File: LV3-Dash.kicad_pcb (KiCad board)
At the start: 2 copper layers, 90 x 50 mm, 93 parts, among them J1 USB_C_Receptacle_USB2.0_16P, J2 FTSH-105-01-L-DV-K-A, J3 Conn_01x04_MountingPin, J4 Conn_01x05_Pin, J5 Conn_01x05_MountingPin, J6 MSD-11-A, J7 62684-401100AHLF, U1 STM32H743VITx, U2 TJA1051T-3, U4 LMR51625YDDCR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

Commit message: more preliminary routing, critical ground
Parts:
- moved D7 0.70 mm to (133.1, 78.4)
- moved F2 0.70 mm to (129.6, 81.6)
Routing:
- net GND: track 0.00 -> 163.3 mm
- net USB-: track 6.85 -> 104.8 mm, vias 1 -> 3
- net USB+: track 5.72 -> 101.4 mm, vias 1 -> 3
- net +3.3V: track 58.1 -> 67.1 mm
- net +5V_BUS: track 32.4 -> 37.2 mm
- net +5V_BUCK: track 13.8 -> 16.0 mm
- net +5V_USB: track 89.0 -> 89.8 mm

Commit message: finalized schematic, some routing
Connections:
- U1 pad 40: unconnected-(U1-PE10-Pad40) -> LCD_EN
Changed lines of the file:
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@@
 	(net 102 "unconnected-(U1-PB5-Pad91)")
 	(net 103 "unconnected-(U1-PE5-Pad4)")
-	(net 104 "unconnected-(U1-PE10-Pad40)")
-	(net 105 "unconnected-(U1-PE7-Pad37)")
-	(net 106 "unconnected-(U1-PB2-Pad36)")
-	(net 107 "unconnected-(U1-PE8-Pad38)")
-	(net 108 "unconnected-(U1-PC14-Pad8)")
-	(net 109 "unconnected-(U1-PA9-Pad68)")
-	(net 110 "unconnected-(U1-PE1-Pad98)")
-	(net 111 "FDCAN2_RX")
-	(net 112 "FDCAN2_TX")
-	(net 113 "unconnected-(U5-NC-Pad4)")
+	(net 104 "unconnected-(U1-PE7-Pad37)")
+	(net 105 "unconnected-(U1-PB2-Pad36)")
+	(net 106 "unconnected-(U1-PE8-Pad38)")
+	(net 107 "unconnected-(U1-PC14-Pad8)")
+	(net 108 "unconnected-(U1-PA9-Pad68)")
+	(net 109 "unconnected-(U1-PE1-Pad98)")
+	(net 110 "FDCAN2_RX")
+	(net 111 "FDCAN2_TX")
+	(net 112 "unconnected-(U5-NC-Pad4)")
 	(footprint "Connector_USB:USB_C_Receptacle_HRO_TYPE-C-31-M-12"
 		(layer "F.Cu")
@@
 			(layers "B.Cu" "B.Mask" "B.Paste")
 			(roundrect_rratio 0.25)
-			(net 108 "unconnected-(U1-PC14-Pad8)")
+			(net 107 "unconnected-(U1-PC14-Pad8)")
 			(pinfunction "PC14")
 			(pintype "bidirectional+no_connect")
@@
 			(layers "B.Cu" "B.Mask" "B.Paste")
 			(roundrect_rratio 0.25)
-			(net 106 "unconnected-(U1-PB2-Pad36)")
+			(net 105 "unconnected-(U1-PB2-Pad36)")
 			(pinfunction "PB2")
 			(pintype "bidirectional+no_connect")
@@
 			(layers "B.Cu" "B.Mask" "B.Paste")
 			(roundrect_rratio 0.25)
-			(net 105 "unconnected-(U1-PE7-Pad37)")
+			(net 104 "unconnected-(U1-PE7-Pad37)")
 			(pinfunction "PE7")
 			(pintype "bidirectional+no_connect")
@@
 			(layers "B.Cu" "B.Mask" "B.Paste")
 			(roundrect_rratio 0.25)
-			(net 107 "unconnected-(U1-PE8-Pad38)")
+			(net 106 "unconnected-(U1-PE8-Pad38)")
 			(pinfunction "PE8")
 			(pintype "bidirectional+no_connect")
@@
 			(layers "B.Cu" "B.Mask" "B.Paste")
 			(roundrect_rratio 0.25)
-			(net 104 "unconnected-(U1-PE10-Pad40)")
+			(net 76 "LCD_EN")
 			(pinfunction "PE10")
-			(pintype "bidirectional+no_connect")
+			(pintype "bidirectional")
 		)
 		(pad "41" smd roundrect
@@
 			(layers "B.Cu" "B.Mask" "B.Paste")
 			(roundrect_rratio 0.25)
-			(net 111 "FDCAN2_RX")
+			(net 110 "FDCAN2_RX")
 			(pinfunction "PB12")
 			(pintype "bidirectional")
@@
 			(layers "B.Cu" "B.Mask" "B.Paste")
 			(roundrect_rratio 0.25)
-			(net 109 "unconnected-(U1-PA9-Pad68)")
+			(net 108 "unconnected-(U1-PA9-Pad68)")
 			(pinfunction "PA9")
 			(pintype "bidirectional+no_connect")
@@
 			(layers "B.Cu" "B.Mask" "B.Paste")
 			(roundrect_rratio 0.25)
-			(net 112 "FDCAN2_TX")
+			(net 111 "FDCAN2_TX")
 			(pinfunction "PB6")
 			(pintype "bidirectional")
@@
 			(layers "B.Cu" "B.Mask" "B.Paste")
 			(roundrect_rratio 0.25)
-			(net 110 "unconnected-(U1-PE1-Pad98)")
+			(net 109 "unconnected-(U1-PE1-Pad98)")
 			(pinfunction "PE1")
 			(pintype "bidirectional+no_connect")
@@
 			(size 0.6 1.2)
 			(layers "B.Cu" "B.Mask" "B.Paste")
-			(net 113 "unconnected-(U5-NC-Pad4)")
+			(net 112 "unconnected-(U5-NC-Pad4)")
 			(pinfunction "NC")
 			(pintype "no_connect")
@@
 			(layers "B.Cu" "B.Mask" "B.Paste")
 			(roundrect_rratio 0.25)
-			(net 112 "FDCAN2_TX")
+			(net 111 "FDCAN2_TX")
 			(pinfunction "TXD")
 			(pintype "input")
@@
 			(layers "B.Cu" "B.Mask" "B.Paste")
 			(roundrect_rratio 0.25)
-			(net 111 "FDCAN2_RX")
+			(net 110 "FDCAN2_RX")
 			(pinfunction "RXD")
 			(pintype "output")

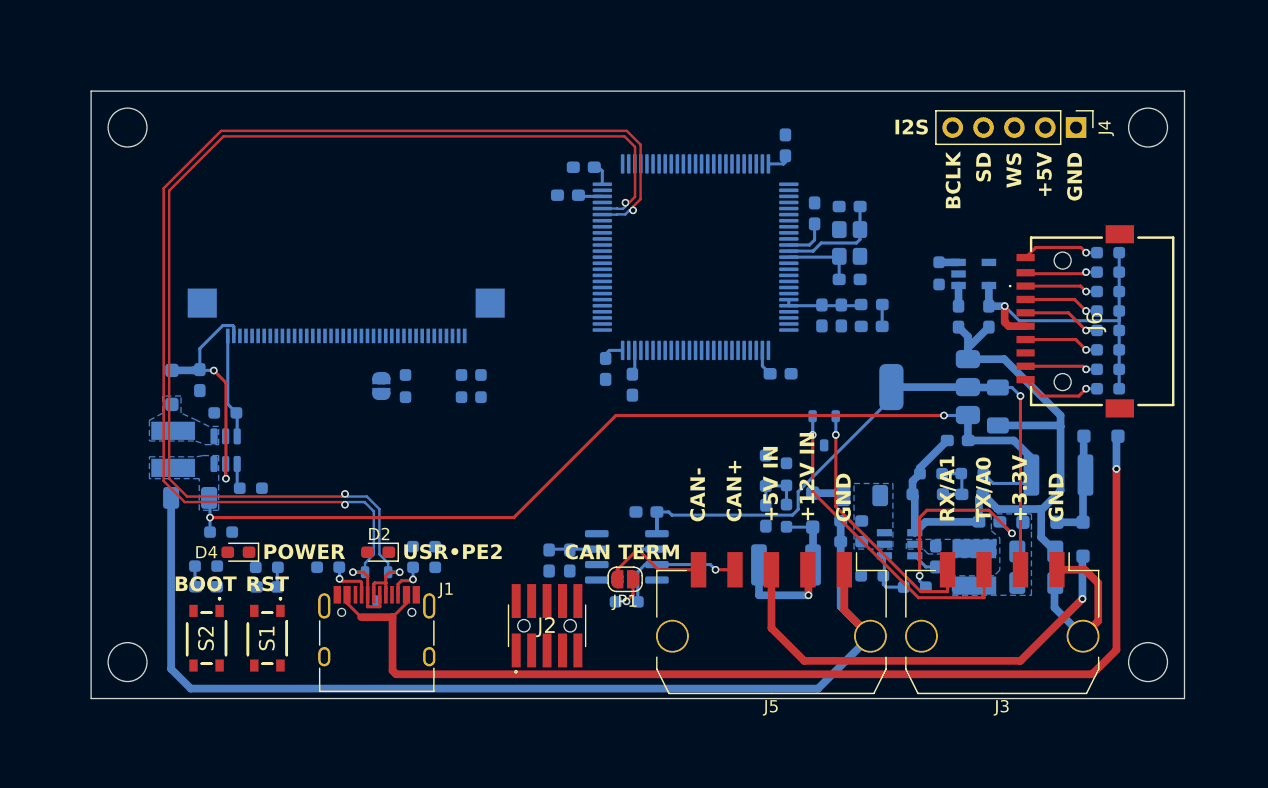
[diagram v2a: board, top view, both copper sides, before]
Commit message: fix duplicate LCD_EN pin, initial ZIF routing
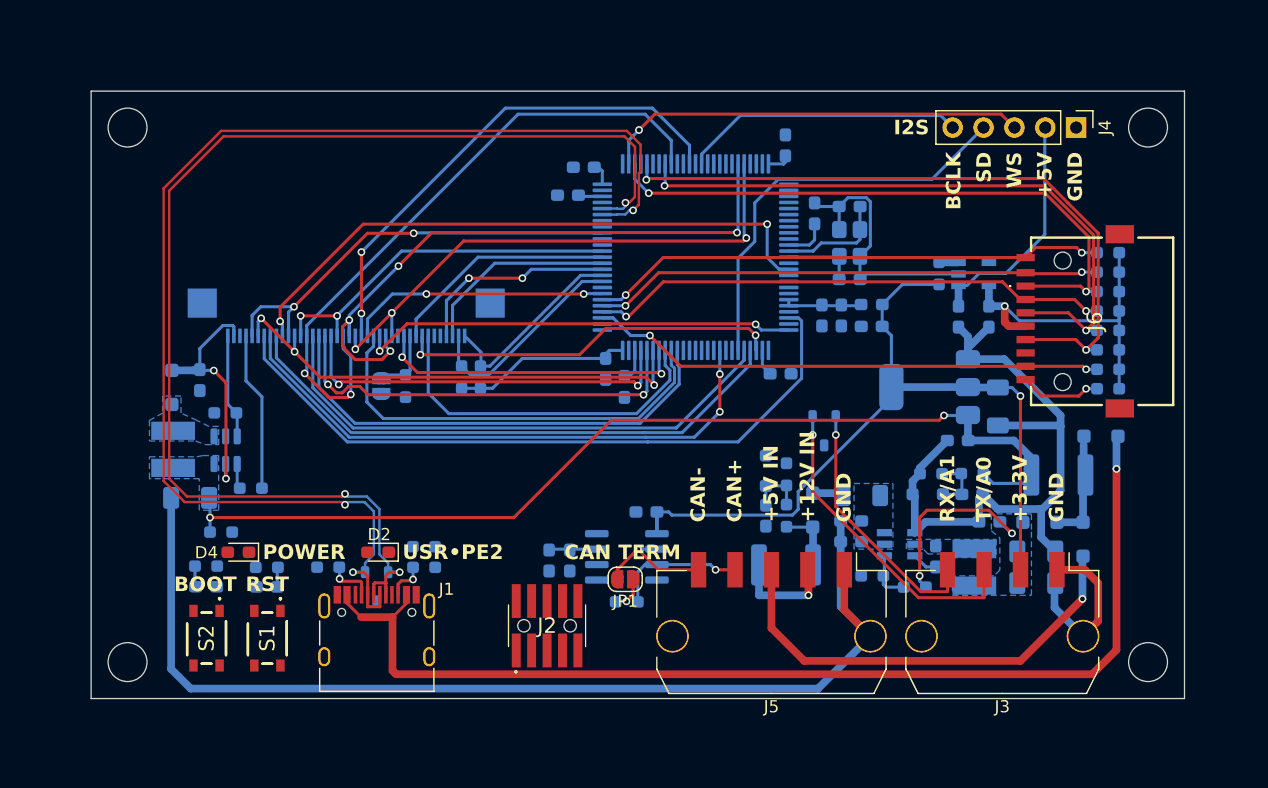
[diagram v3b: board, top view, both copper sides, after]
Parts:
- moved R26 0.73 mm to (82.0, 73.5)
- moved R27 0.73 mm to (80.5, 73.5)
- moved C13 0.68 mm to (93.9, 74.3)
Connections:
- U1 pad 58: LCD_EN -> unconnected-(U1-PD11-Pad58)
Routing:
- net LCD_R2: track 0.00 -> 57.0 mm
- net LCD_G7: track 0.00 -> 53.9 mm, vias 0 -> 2
- net LCD_B6: track 0.00 -> 51.9 mm, vias 0 -> 4
- net SD_CLK: track 6.23 -> 56.7 mm, vias 1 -> 2
- net LCD_R5: track 0.00 -> 50.3 mm, vias 0 -> 2
- net LCD_R3: track 0.00 -> 47.5 mm, vias 0 -> 2
- net SD_CMD: track 6.48 -> 53.4 mm, vias 1 -> 2
- net LCD_R4: track 0.00 -> 46.8 mm
- net SD_D2: track 6.06 -> 51.3 mm, vias 1 -> 2
- net LCD_B7: track 0.00 -> 45.2 mm, vias 0 -> 3
- net LCD_G2: track 0.00 -> 44.3 mm
- net LCD_B2: track 0.00 -> 41.6 mm, vias 0 -> 2
- net LCD_R7: track 0.00 -> 40.4 mm, vias 0 -> 3
- net LCD_G3: track 0.00 -> 39.3 mm
- net SD_CS: track 6.27 -> 43.1 mm, vias 1 -> 2
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
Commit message: initial routing of all signals, 5v 3.3v not done
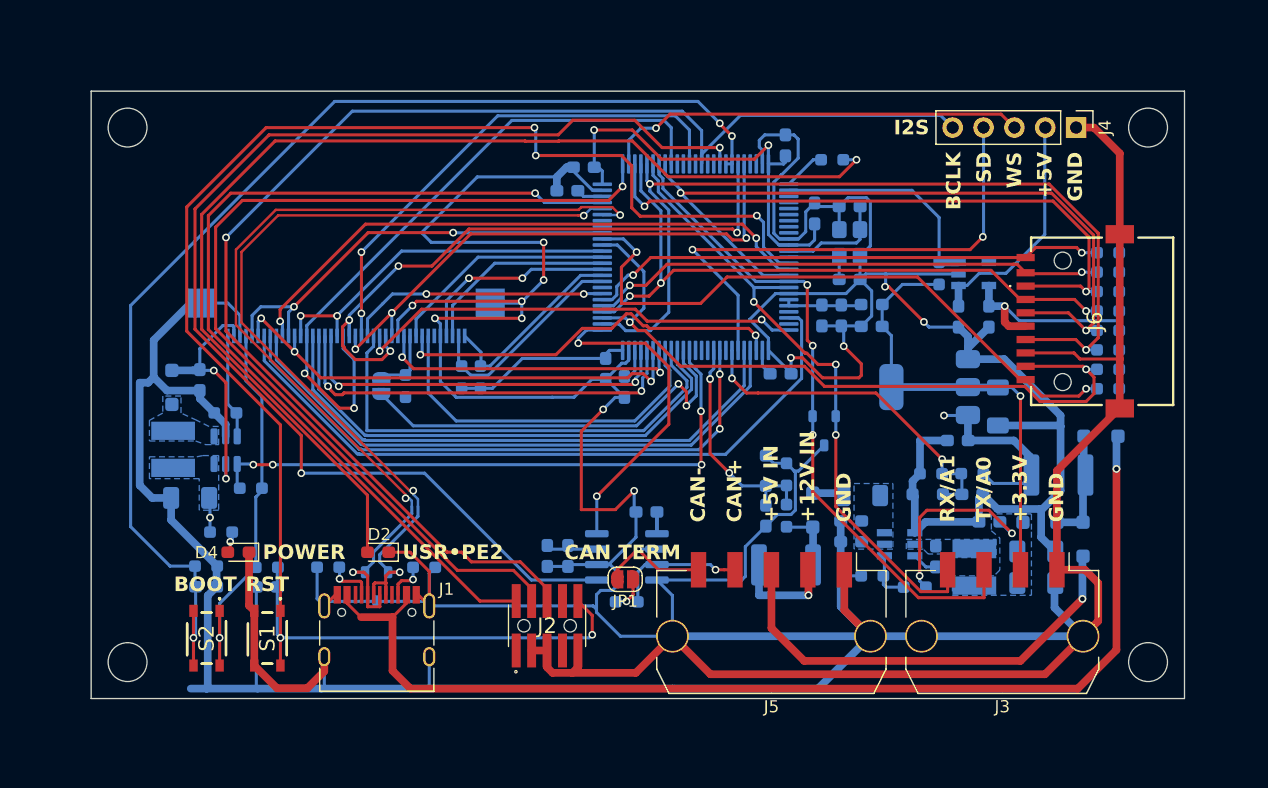
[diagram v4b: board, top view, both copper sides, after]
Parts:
- moved R5 46.3 mm to (111.0, 55.6), turned to 0 degrees
- moved C15 0.40 mm to (89.2, 88.3)
- moved C16 0.40 mm to (87.5, 88.3)
- moved C14 0.37 mm to (89.2, 58.2)
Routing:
- net GND: track 185.4 -> 653.0 mm, vias 0 -> 12
- net NRST: track 1.64 -> 137.3 mm, vias 0 -> 5
- net FDCAN2_TX: track 0.00 -> 101.8 mm, vias 0 -> 2
- net BOOT0: track 1.72 -> 95.8 mm, vias 0 -> 3
- net Net-(D2-A): track 0.00 -> 92.8 mm, vias 0 -> 1
- net I2S_BCLK: track 23.2 -> 114.0 mm, vias 0 -> 1
- net SWD_CLK: track 0.00 -> 81.0 mm, vias 0 -> 1
- net SWD_IO: track 0.00 -> 77.5 mm, vias 0 -> 1
- net +5V: track 106.1 -> 42.5 mm
- net BKLT_CTRL: track 2.08 -> 50.2 mm, vias 0 -> 4
- net SD_D1: track 6.69 -> 52.4 mm, vias 1 -> 2
- net LCD_EN: track 0.00 -> 34.4 mm, vias 0 -> 2
- net DPAD_A1: track 21.3 -> 52.2 mm, vias 1 -> 3
- net USB+: track 101.4 -> 71.1 mm
- net USB-: track 104.8 -> 76.0 mm
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
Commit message: fully routed, needs cleanup, planes
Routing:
- net +3.3V: track 125.1 -> 239.8 mm, vias 4 -> 14
- net +5V: track 42.5 -> 122.6 mm, vias 2 -> 6
- net LCD_B7: track 45.6 -> 44.9 mm
- net LCD_B6: track 52.2 -> 51.6 mm
- net GND: track 653.0 -> 653.5 mm, vias 12 -> 13

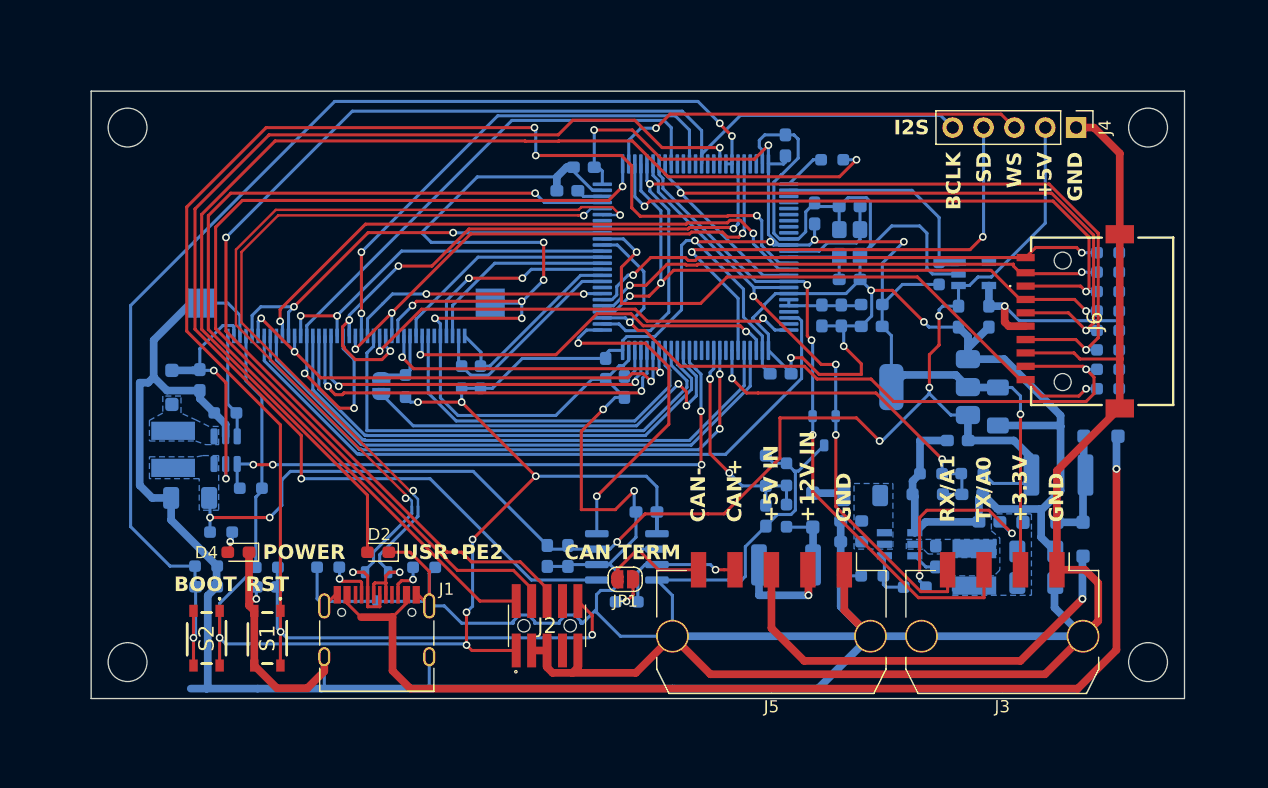
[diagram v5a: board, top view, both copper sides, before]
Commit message: trace cleanup, ground planes, silkscreen cleanup
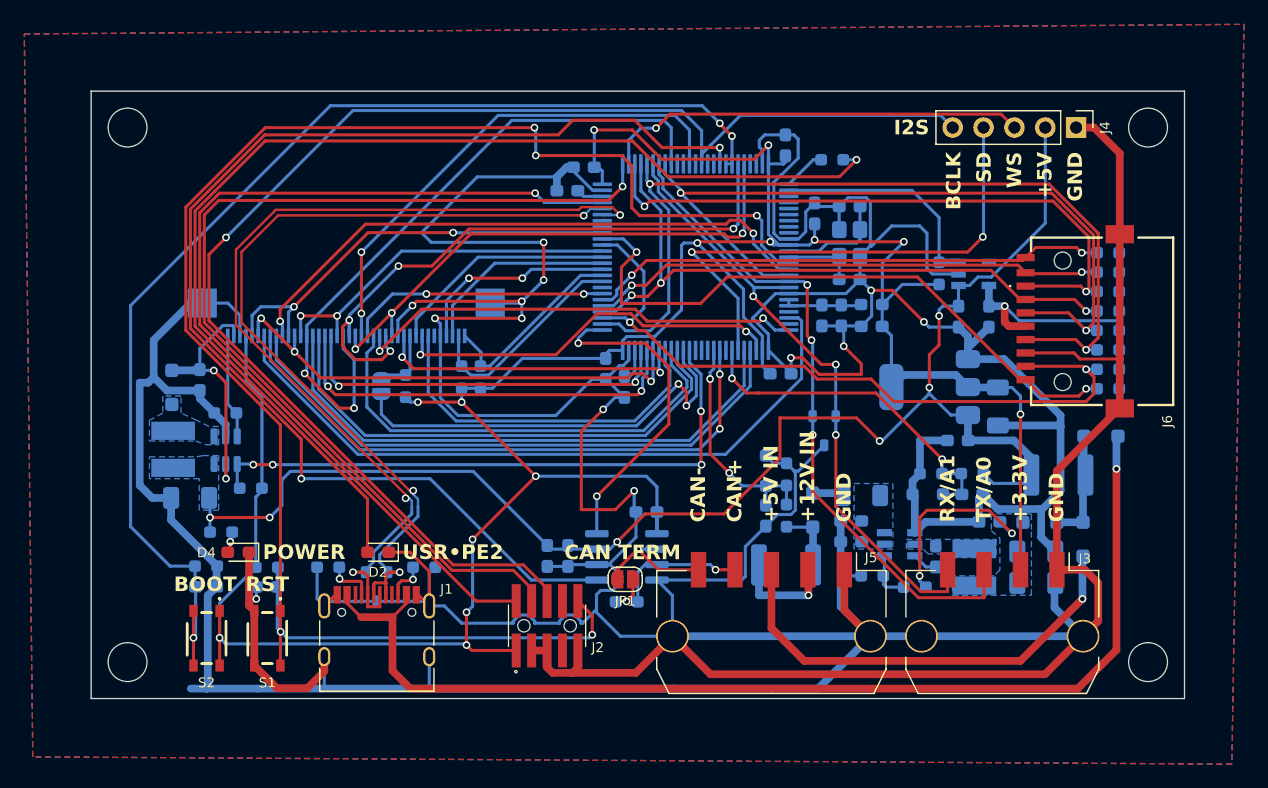
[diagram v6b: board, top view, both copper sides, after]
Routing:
- net SWD_CLK: track 81.0 -> 83.2 mm
- net I2S_BCLK: track 114.0 -> 115.5 mm
- net SWD_IO: track 77.5 -> 78.8 mm
- net LCD_B4: track 39.4 -> 38.3 mm
- net LCD_EN: track 34.4 -> 35.4 mm
- net Net-(D2-A): track 92.8 -> 93.7 mm
- net FDCAN2_TX: track 102.1 -> 102.6 mm
- added copper zone on B.Cu, net GND
- added copper zone on F.Cu, net GND

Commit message: fillets, graphics, other fixes
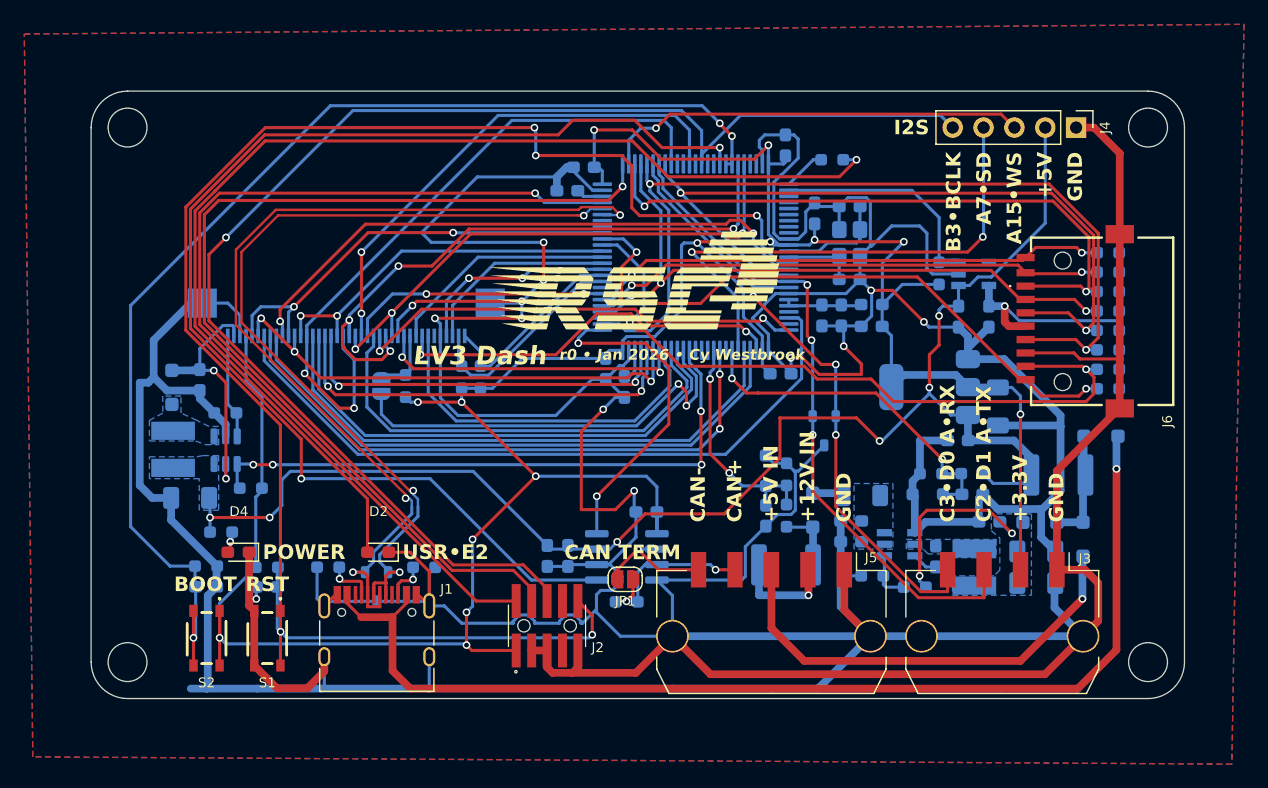
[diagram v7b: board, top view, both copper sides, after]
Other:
- outline, holes or cut-outs redrawn
- board text added: "A15•WS"
- board text added: "A7•SD"
- board text added: "B3•BCLK"
- board text added: "C2•D1 A•TX"
- board text added: "C3•D0 A•RX"
- board text added: "LV3 Dash"
- board text added: "USR•E2"
- board text added: "r0 • Jan 2026 Cy Westbrook"
- board text added: "r0 • Jan 2026 • Cy Westbrook"
- board text removed: "BCLK"
- board text removed: "RX/A1"
- board text removed: "SD"
- board text removed: "TX/A0"
- board text removed: "USR•PE2"
- board text removed: "WS"

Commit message: FINAL FOR ORDER (4 Jan 2026)
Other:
- board text added: "*shared with ITM/SWO"
- board text added: "B3•BCLK*"
- board text added: "C2/D1•TX"
- board text added: "C3/D0•RX"
- board text removed: "B3•BCLK"
- board text removed: "C2•D1 A•TX"
- board text removed: "C3•D0 A•RX"
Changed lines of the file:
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@@
 		(layer "Edge.Cuts")
 	)
-	(gr_text "C3•D0 A•RX"
+	(gr_text "C3/D0•RX"
 		(at 120.5 85.5 90)
 		(layer "F.SilkS")
@@
 		)
 	)
-	(gr_text "B3•BCLK"
+	(gr_text "B3•BCLK*"
 		(at 121 55 90)
 		(layer "F.SilkS")
@@
 	)
 	(gr_text "LV3 Dash"
-		(at 76.453204 71.780286 0)
+		(at 77.953204 71.780286 0)
 		(layer "F.SilkS" knockout)
 		(effects
@@
 		)
 	)
+	(gr_text "*shared with ITM/SWO"
+		(at 106 53 0)
+		(layer "F.SilkS")
+		(effects
+			(font
+				(size 0.8128 0.8128)
+				(thickness 0.1524)
+			)
+		)
+	)
 	(gr_text "A15•WS"
 		(at 126 55 90)
@@
 		)
 	)
-	(gr_text "C2•D1 A•TX"
+	(gr_text "C2/D1•TX"
 		(at 123.490105 85.489277 90)
 		(layer "F.SilkS")
@@
 	)
 	(gr_text "r0 • Jan 2026 • Cy Westbrook"
-		(at 88.5 71.7 0)
+		(at 90 71.7 0)
 		(layer "F.SilkS")
 		(effects
@@
 			)
 			(justify right)
+		)
+	)
+	(gr_text "A15•WS"
+		(at 126 55 90)
+		(layer "B.SilkS")
+		(effects
+			(font
+				(size 0.8 0.8)
+				(thickness 0.18)
+				(bold yes)
+			)
+			(justify left mirror)
+		)
+	)
+	(gr_text "GND"
+		(at 131 55 90)
+		(layer "B.SilkS")
+		(effects
+			(font
+				(size 0.8 0.8)
+				(thickness 0.18)
+				(bold yes)
+			)
+			(justify left mirror)
+		)
+	)
+	(gr_text "A7•SD"
+		(at 123.5 55 90)
+		(layer "B.SilkS")
+		(effects
+			(font
+				(size 0.8 0.8)
+				(thickness 0.18)
+				(bold yes)
+			)
+			(justify left mirror)
+		)
+	)
+	(gr_text "+5V"
+		(at 128.5 55 90)
+		(layer "B.SilkS")
+		(effects
+			(font
+				(size 0.8 0.8)
+				(thickness 0.18)
+				(bold yes)
+			)
+			(justify left mirror)
 		)
 	)
@@
 				(bold yes)
 				(italic yes)
+			)
+			(justify left mirror)
+		)
+	)
+	(gr_text "B3•BCLK*"
+		(at 121 55 90)
+		(layer "B.SilkS")
+		(effects
+			(font
+				(size 0.8 0.8)
+				(thickness 0.18)
+				(bold yes)
 			)
 			(justify left mirror)
@@
 			(keep_text_aligned yes)
 		)
-		(gr_text "3543.3071"
+		(gr_text "90"
 			(at 95.000001 116.417404 0)
 			(layer "Dwgs.User")
@@
 			(keep_text_aligned yes)
 		)
-		(gr_text "944.8819"
+		(gr_text "24"
 			(at 83.008506 33.056491 0)
 			(layer "Dwgs.User")
@@
 			(keep_text_aligned yes)
 		)
-		(gr_text "1771.6536"
+		(gr_text "45"
 			(at 72.500001 109.417404 0)
 			(layer "Dwgs.User")
@@
 			(keep_text_aligned yes)
 		)
-		(gr_text "1279.5276"
+		(gr_text "32.5"
 			(at 41.35 83.959962 90)
 			(layer "Dwgs.User")
